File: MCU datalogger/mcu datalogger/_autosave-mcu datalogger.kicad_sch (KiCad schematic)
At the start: 23 parts, among them U1 24LC1025, U2 24LC1025, U3 DS1337S_, U4 ATMEGA328P-AU, Y1 Crystal, Y2 Crystal

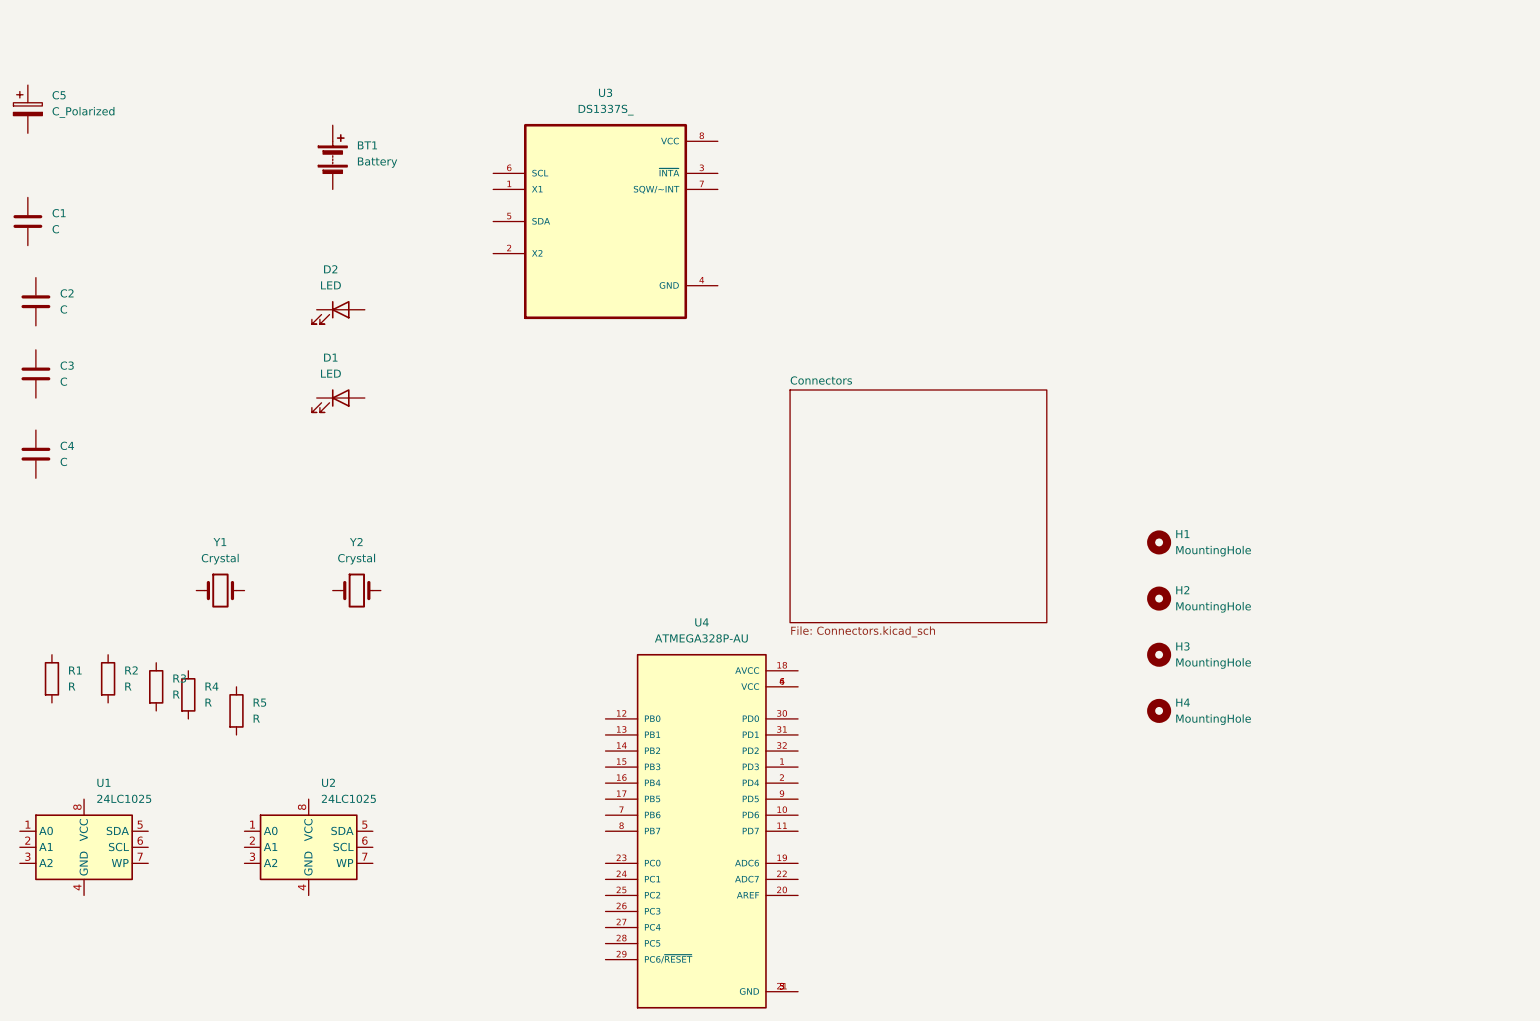
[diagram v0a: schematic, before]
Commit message: Added 2 more resitors and assembled the symbols accordingly.
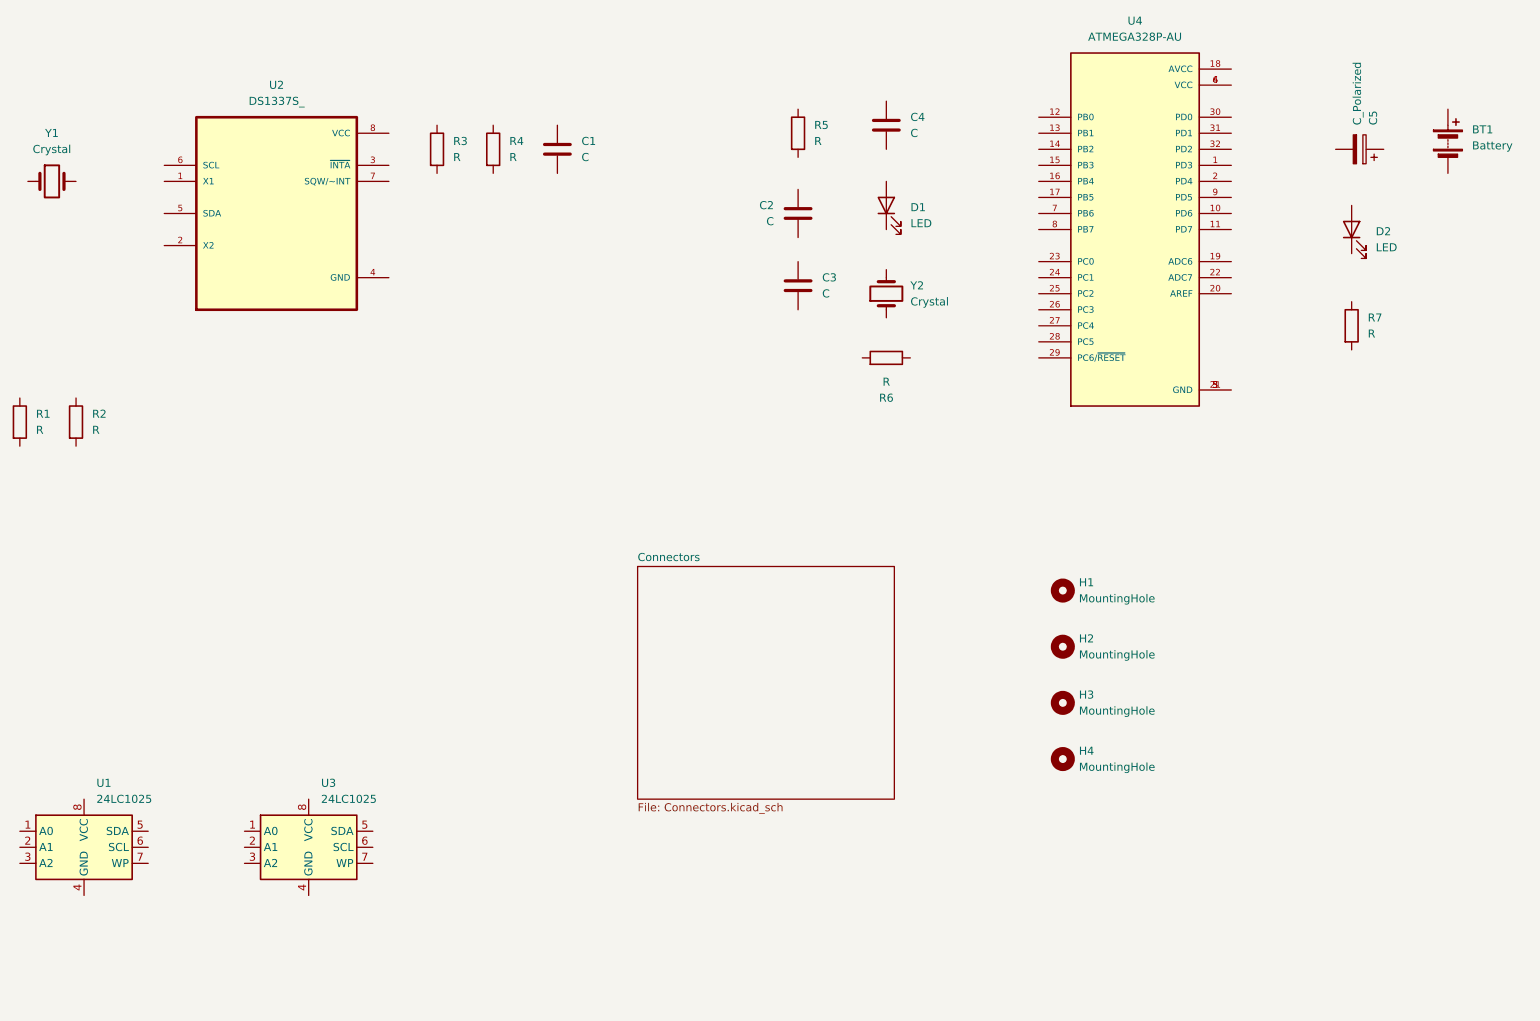
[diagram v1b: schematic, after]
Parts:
- added R5, R7: R, symbol Device:R
- renumbered C4 to C1, C1 to C4, R4 to R3, R5 to R4, R3 to R6, U3 to U2, U2 to U3
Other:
- moved on the sheet: BT1, C1, C2, C3, C4, C5, D1, D2, H1, H2, H3, H4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
